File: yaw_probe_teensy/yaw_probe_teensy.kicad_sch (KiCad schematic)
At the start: 18 parts, among them J1 CAN Connection, J2 DRS Button 1, J3 DRS Button 2, J4 DRS Output, U1 Teensy4.0, U2 MS4525DO, U3 MS4525DO, U4 SN65HVD230_CAN_Transceiver

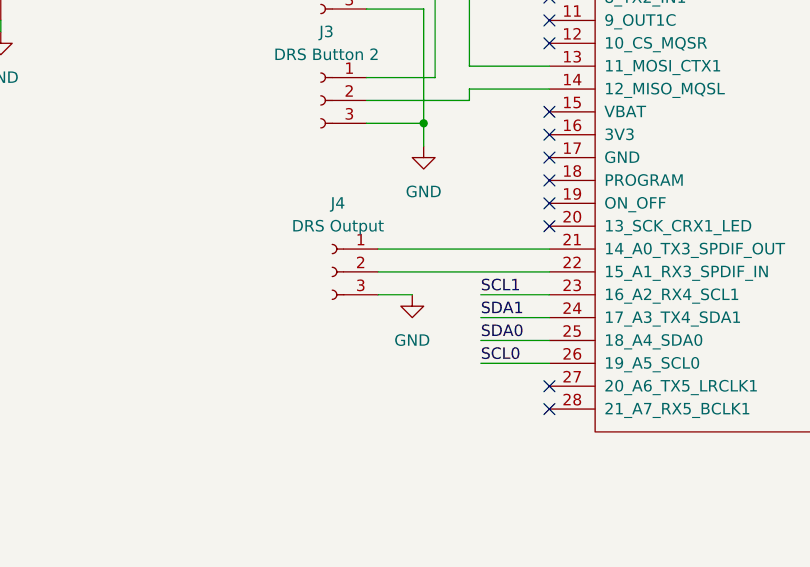
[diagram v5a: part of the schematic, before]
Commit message: add another pwm output to aero board
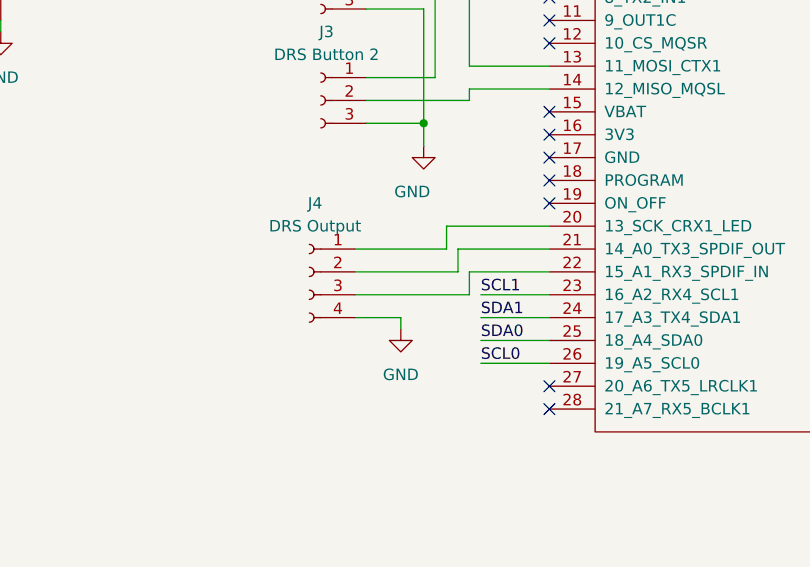
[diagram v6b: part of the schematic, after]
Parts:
- removed J4: DRS Output, TerminalBlock_TE-Connectivity:TerminalBlock_TE_282834-3_1x03_P2.54mm_Horizontal, symbol Connector:Conn_01x03_Female
- added J4: DRS Output, TerminalBlock_TE-Connectivity:TerminalBlock_TE_282834-4_1x04_P2.54mm_Horizontal, symbol Connector:Conn_01x04_Female
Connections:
- net GND: now also J4.4 (Pin_4)
- net at U1.21 (14_A0_TX3_SPDIF_OUT): now also J4.2 (Pin_2)
- net at U1.22 (15_A1_RX3_SPDIF_IN): now also J4.3 (Pin_3)
- net at U1.20 (13_SCK_CRX1_LED): now also J4.1 (Pin_1)
- no-connect marks 48 -> 47
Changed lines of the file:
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@@
   (title_block
     (title "SDM-23 Aero Board")
-    (date "2023-01-11")
+    (date "2023-01-13")
     (rev "v1")
     (company "Sun Devil Motorsports")
@@
   (no_connect (at 175.26 93.98))
   (no_connect (at 207.01 59.69))
-  (no_connect (at 119.38 96.52))
   (no_connect (at 175.26 81.28))
   (no_connect (at 175.26 63.5))
@@
     (stroke (width 0) (type default) (color 0 0 0 0))
   )
-  (wire (pts (xy 100.33 99.06) (xy 119.38 99.06))
-    (stroke (width 0) (type default) (color 0 0 0 0))
-  )
   (wire (pts (xy 110.49 82.55) (xy 99.06 82.55))
     (stroke (width 0) (type default) (color 0 0 0 0))
   )
+  (wire (pts (xy 119.38 99.06) (xy 109.22 99.06))
+    (stroke (width 0) (type default) (color 0 0 0 0))
+  )
+  (wire (pts (xy 102.87 107.95) (xy 102.87 106.68))
+    (stroke (width 0) (type default) (color 0 0 0 0))
+  )
   (wire (pts (xy 214.63 114.3) (xy 228.6 114.3))
     (stroke (width 0) (type default) (color 0 0 0 0))
@@
     (stroke (width 0) (type default) (color 0 0 0 0))
   )
+  (wire (pts (xy 102.87 106.68) (xy 97.79 106.68))
+    (stroke (width 0) (type default) (color 0 0 0 0))
+  )
   (wire (pts (xy 233.68 71.12) (xy 233.68 67.31))
     (stroke (width 0) (type default) (color 0 0 0 0))
@@
     (stroke (width 0) (type default) (color 0 0 0 0))
   )
+  (wire (pts (xy 97.79 101.6) (xy 109.22 101.6))
+    (stroke (width 0) (type default) (color 0 0 0 0))
+  )
   (wire (pts (xy 68.58 68.58) (xy 72.39 68.58))
     (stroke (width 0) (type default) (color 0 0 0 0))
   )
-  (wire (pts (xy 100.33 104.14) (xy 104.14 104.14))
-    (stroke (width 0) (type default) (color 0 0 0 0))
-  )
   (wire (pts (xy 220.98 62.23) (xy 232.41 62.23))
     (stroke (width 0) (type default) (color 0 0 0 0))
@@
     (stroke (width 0) (type default) (color 0 0 0 0))
   )
+  (wire (pts (xy 107.95 96.52) (xy 107.95 99.06))
+    (stroke (width 0) (type default) (color 0 0 0 0))
+  )
   (wire (pts (xy 60.96 44.45) (xy 68.58 44.45))
     (stroke (width 0) (type default) (color 0 0 0 0))
   )
+  (wire (pts (xy 110.49 104.14) (xy 110.49 101.6))
+    (stroke (width 0) (type default) (color 0 0 0 0))
+  )
   (wire (pts (xy 175.26 106.68) (xy 180.34 106.68))
     (stroke (width 0) (type default) (color 0 0 0 0))
@@
     (stroke (width 0) (type default) (color 0 0 0 0))
   )
+  (wire (pts (xy 109.22 99.06) (xy 109.22 101.6))
+    (stroke (width 0) (type default) (color 0 0 0 0))
+  )
   (wire (pts (xy 215.9 124.46) (xy 214.63 124.46))
     (stroke (width 0) (type default) (color 0 0 0 0))
   )
+  (wire (pts (xy 107.95 96.52) (xy 119.38 96.52))
+    (stroke (width 0) (type default) (color 0 0 0 0))
+  )
   (wire (pts (xy 119.38 78.74) (xy 110.49 78.74))
     (stroke (width 0) (type default) (color 0 0 0 0))
@@
     (stroke (width 0) (type default) (color 0 0 0 0))
   )
+  (wire (pts (xy 110.49 101.6) (xy 119.38 101.6))
+    (stroke (width 0) (type default) (color 0 0 0 0))
+  )
+  (wire (pts (xy 97.79 104.14) (xy 110.49 104.14))
+    (stroke (width 0) (type default) (color 0 0 0 0))
+  )
   (wire (pts (xy 210.82 114.3) (xy 214.63 114.3))
     (stroke (width 0) (type default) (color 0 0 0 0))
@@
     (stroke (width 0) (type default) (color 0 0 0 0))
   )
-  (wire (pts (xy 100.33 101.6) (xy 119.38 101.6))
-    (stroke (width 0) (type default) (color 0 0 0 0))
-  )
   (wire (pts (xy 222.25 92.71) (xy 224.79 92.71))
     (stroke (width 0) (type default) (color 0 0 0 0))
@@
   )
   (wire (pts (xy 35.56 69.85) (xy 44.45 69.85))
+    (stroke (width 0) (type default) (color 0 0 0 0))
+  )
+  (wire (pts (xy 97.79 99.06) (xy 107.95 99.06))
     (stroke (width 0) (type default) (color 0 0 0 0))
   )
@@
     (pin "1")
   )
-  (symbol (lib_id "Connector:Conn_01x03_Female") (at 95.25 101.6 0) (mirror y) (unit 1)
-    (in_bom yes) (on_board yes) (fields_autoplaced)
-    (property "Reference" "J4" (id 0) (at 95.885 93.98 0))
-    (property "Value" "DRS Output" (id 1) (at 95.885 96.52 0))
-    (property "Footprint" "TerminalBlock_TE-Connectivity:TerminalBlock_TE_282834-3_1x03_P2.54mm_Horizontal" (id 2) (at 95.25 101.6 0)
-      (effects (font (size 1.27 1.27)) hide)
-    )
-    (property "Datasheet" "~" (id 3) (at 95.25 101.6 0)
-      (effects (font (size 1.27 1.27)) hide)
-    )
-    (pin "1")
-    (pin "2")
-    (pin "3")
-  )
   (symbol (lib_id "power:+3.3V") (at 242.57 62.23 0) (unit 1)
     (in_bom yes) (on_board yes) (fields_autoplaced)
@@
   )
   (symbol (lib_id "power:GND") (at 105.41 87.63 0) (unit 1)
-    (in_bom yes) (on_board yes) (fields_autoplaced)
+    (in_bom yes) (on_board yes)
     (property "Reference" "#PWR0114" (id 0) (at 105.41 93.98 0)
       (effects (font (size 1.27 1.27)) hide)
     )
-    (property "Value" "GND" (id 1) (at 105.41 92.71 0))
+    (property "Value" "GND" (id 1) (at 104.14 92.71 0))
     (property "Footprint" "" (id 2) (at 105.41 87.63 0)
       (effects (font (size 1.27 1.27)) hide)
@@
     (pin "1")
   )
-  (symbol (lib_id "power:GND") (at 104.14 104.14 0) (unit 1)
-    (in_bom yes) (on_board yes) (fields_autoplaced)
-    (property "Reference" "#PWR0113" (id 0) (at 104.14 110.49 0)
-      (effects (font (size 1.27 1.27)) hide)
-    )
-    (property "Value" "GND" (id 1) (at 104.14 109.22 0))
-    (property "Footprint" "" (id 2) (at 104.14 104.14 0)
-      (effects (font (size 1.27 1.27)) hide)
-    )
-    (property "Datasheet" "" (id 3) (at 104.14 104.14 0)
+  (symbol (lib_id "power:GND") (at 102.87 107.95 0) (unit 1)
+    (in_bom yes) (on_board yes) (fields_autoplaced)
+    (property "Reference" "#PWR0113" (id 0) (at 102.87 114.3 0)
+      (effects (font (size 1.27 1.27)) hide)
+    )
+    (property "Value" "GND" (id 1) (at 102.87 113.03 0))
+    (property "Footprint" "" (id 2) (at 102.87 107.95 0)
+      (effects (font (size 1.27 1.27)) hide)
+    )
+    (property "Datasheet" "" (id 3) (at 102.87 107.95 0)
       (effects (font (size 1.27 1.27)) hide)
     )
@@
     (pin "1")
   )
+  (symbol (lib_id "Connector:Conn_01x04_Female") (at 92.71 101.6 0) (mirror y) (unit 1)
+    (in_bom yes) (on_board yes) (fields_autoplaced)
+    (property "Reference" "J4" (id 0) (at 93.345 93.98 0))
+    (property "Value" "DRS Output" (id 1) (at 93.345 96.52 0))
+    (property "Footprint" "TerminalBlock_TE-Connectivity:TerminalBlock_TE_282834-4_1x04_P2.54mm_Horizontal" (id 2) (at 92.71 101.6 0)
+      (effects (font (size 1.27 1.27)) hide)
+    )
+    (property "Datasheet" "~" (id 3) (at 92.71 101.6 0)
+      (effects (font (size 1.27 1.27)) hide)
+    )
+    (pin "1")
+    (pin "2")
+    (pin "3")
+    (pin "4")
+  )
   (symbol (lib_id "Connector:Conn_01x04_Female") (at 55.88 44.45 0) (mirror y) (unit 1)
     (in_bom yes) (on_board yes) (fields_autoplaced)
@@
       (reference "J3") (unit 1) (value "DRS Button 2") (footprint "TerminalBlock_TE-Connectivity:TerminalBlock_TE_282834-3_1x03_P2.54mm_Horizontal")
     )
-    (path "/2582dcff-8958-46a5-8ab8-b702a608c6a4"
-      (reference "J4") (unit 1) (value "DRS Output") (footprint "TerminalBlock_TE-Connectivity:TerminalBlock_TE_282834-3_1x03_P2.54mm_Horizontal")
+    (path "/df9cfb14-95e1-4608-b124-6c944114fd01"
+      (reference "J4") (unit 1) (value "DRS Output") (footprint "TerminalBlock_TE-Connectivity:TerminalBlock_TE_282834-4_1x04_P2.54mm_Horizontal")
     )
     (path "/8fca02e5-2732-483b-ad1a-a78a92441fab"

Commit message: start sg amplifier
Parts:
- removed C1, C2: 100nF, Capacitor_THT:C_Disc_D3.0mm_W1.6mm_P2.50mm, symbol Device:C_Small
- removed U2, U3: MS4525DO, SDM:MS4525-DSvoxxxyP, symbol SDM:MS4525DO
- added J5: Air Speed, Connector_JST:JST_GH_BM04B-GHS-TBT_1x04-1MP_P1.25mm_Vertical, symbol Connector:Conn_01x04_Female
- added J6: Yaw, Connector_JST:JST_GH_BM04B-GHS-TBT_1x04-1MP_P1.25mm_Vertical, symbol Connector:Conn_01x04_Female
- H1, H2, H3, H4: value MountingHole -> M3
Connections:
- net GND: now also J5.1 (Pin_1), J6.1 (Pin_1)
- net SCL0: now also J5.3 (Pin_3)
- net SCL1: now also J6.3 (Pin_3)
- net SDA0: now also J5.2 (Pin_2)
- net SDA1: now also J6.2 (Pin_2)
- net VCC: now also J5.4 (Pin_4), J6.4 (Pin_4)
- no-connect marks 47 -> 39
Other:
- note added: "VCC = 5V"
- company: Sun Devil Motorsports -> (none)
- moved on the sheet: H1, H2, H3, H4

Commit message: various improvements
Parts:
- removed J2: DRS Button 1, TerminalBlock_TE-Connectivity:TerminalBlock_TE_282834-3_1x03_P2.54mm_Horizontal, symbol Connector:Conn_01x03_Female
- removed J3: DRS Button 2, TerminalBlock_TE-Connectivity:TerminalBlock_TE_282834-3_1x03_P2.54mm_Horizontal, symbol Connector:Conn_01x03_Female
- removed J4: DRS Output, TerminalBlock_TE-Connectivity:TerminalBlock_TE_282834-4_1x04_P2.54mm_Horizontal, symbol Connector:Conn_01x04_Female
- J5, J6: footprint Connector_JST:JST_GH_BM04B-GHS-TBT_1x04-1MP_P1.25mm_Vertical -> TerminalBlock_TE-Connectivity:TerminalBlock_TE_282834-4_1x04_P2.54mm_Horizontal
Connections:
- net SCL0: now also J5.2 (Pin_2); no longer J5.3 (Pin_3)
- net SDA0: now also J5.3 (Pin_3); no longer J5.2 (Pin_2)
- no-connect marks 39 -> 44
